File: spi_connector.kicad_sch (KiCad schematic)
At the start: 4 parts

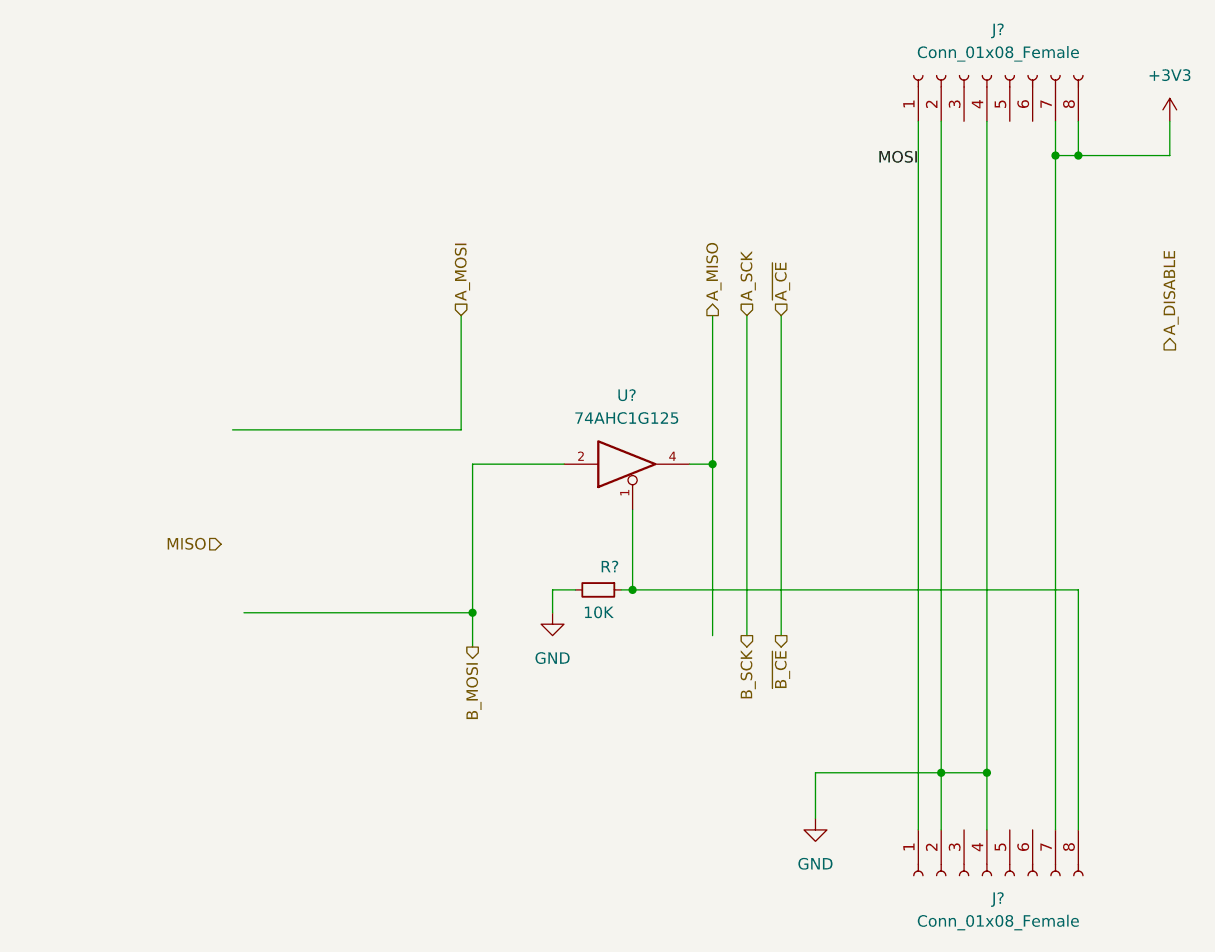
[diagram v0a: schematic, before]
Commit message: Schematic: Improve spi connector
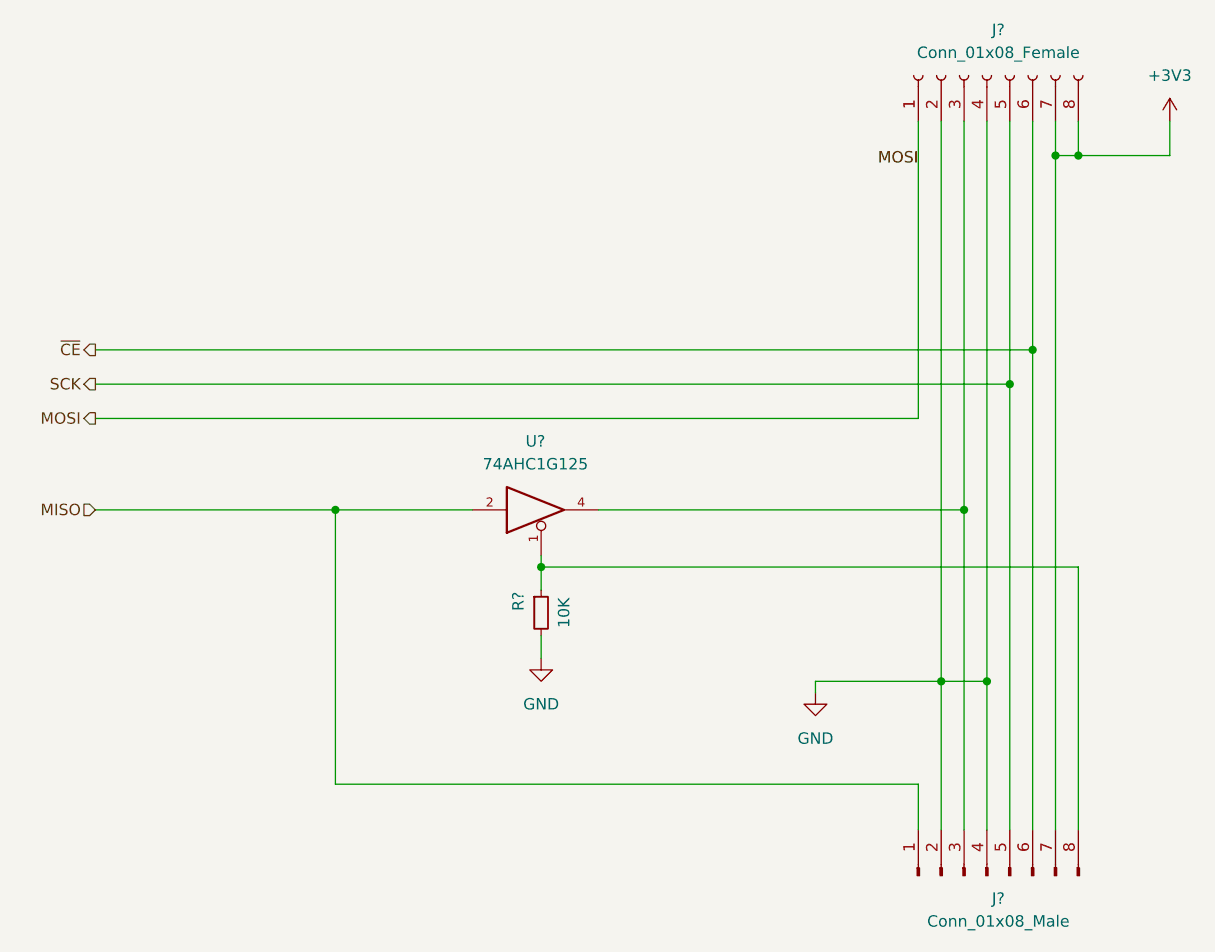
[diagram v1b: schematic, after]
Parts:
- removed J?: Conn_01x08_Female, symbol Connector:Conn_01x08_Female
- added J?: Conn_01x08_Male, symbol Connector:Conn_01x08_Male
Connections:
- net A_MISO is gone; now on an unnamed net: U?.4
- net B_MOSI is gone; now on net MISO: U?.2
- net +3V3: now also J?.7 (Pin_7)
- net GND: now also J?.2 (Pin_2), J?.4 (Pin_4)
- net MISO: now also J?.1 (Pin_1)
- net at R?.1, U?.1: now also J?.8 (Pin_8)
- net at J?.3 (Pin_3): now also J?.3 (Pin_3)
- net SCK: now reaches J?.5 (Pin_5)
- net SCK: now also J?.5 (Pin_5)
- net ~{CE}: now reaches J?.6 (Pin_6)
- net ~{CE}: now also J?.6 (Pin_6)
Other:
- moved on the sheet: R?, U?
